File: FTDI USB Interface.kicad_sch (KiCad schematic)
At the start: 31 parts, among them U3 93LCxxA, U4 ASDMB-xxxMHz, U5 FT2232HQ

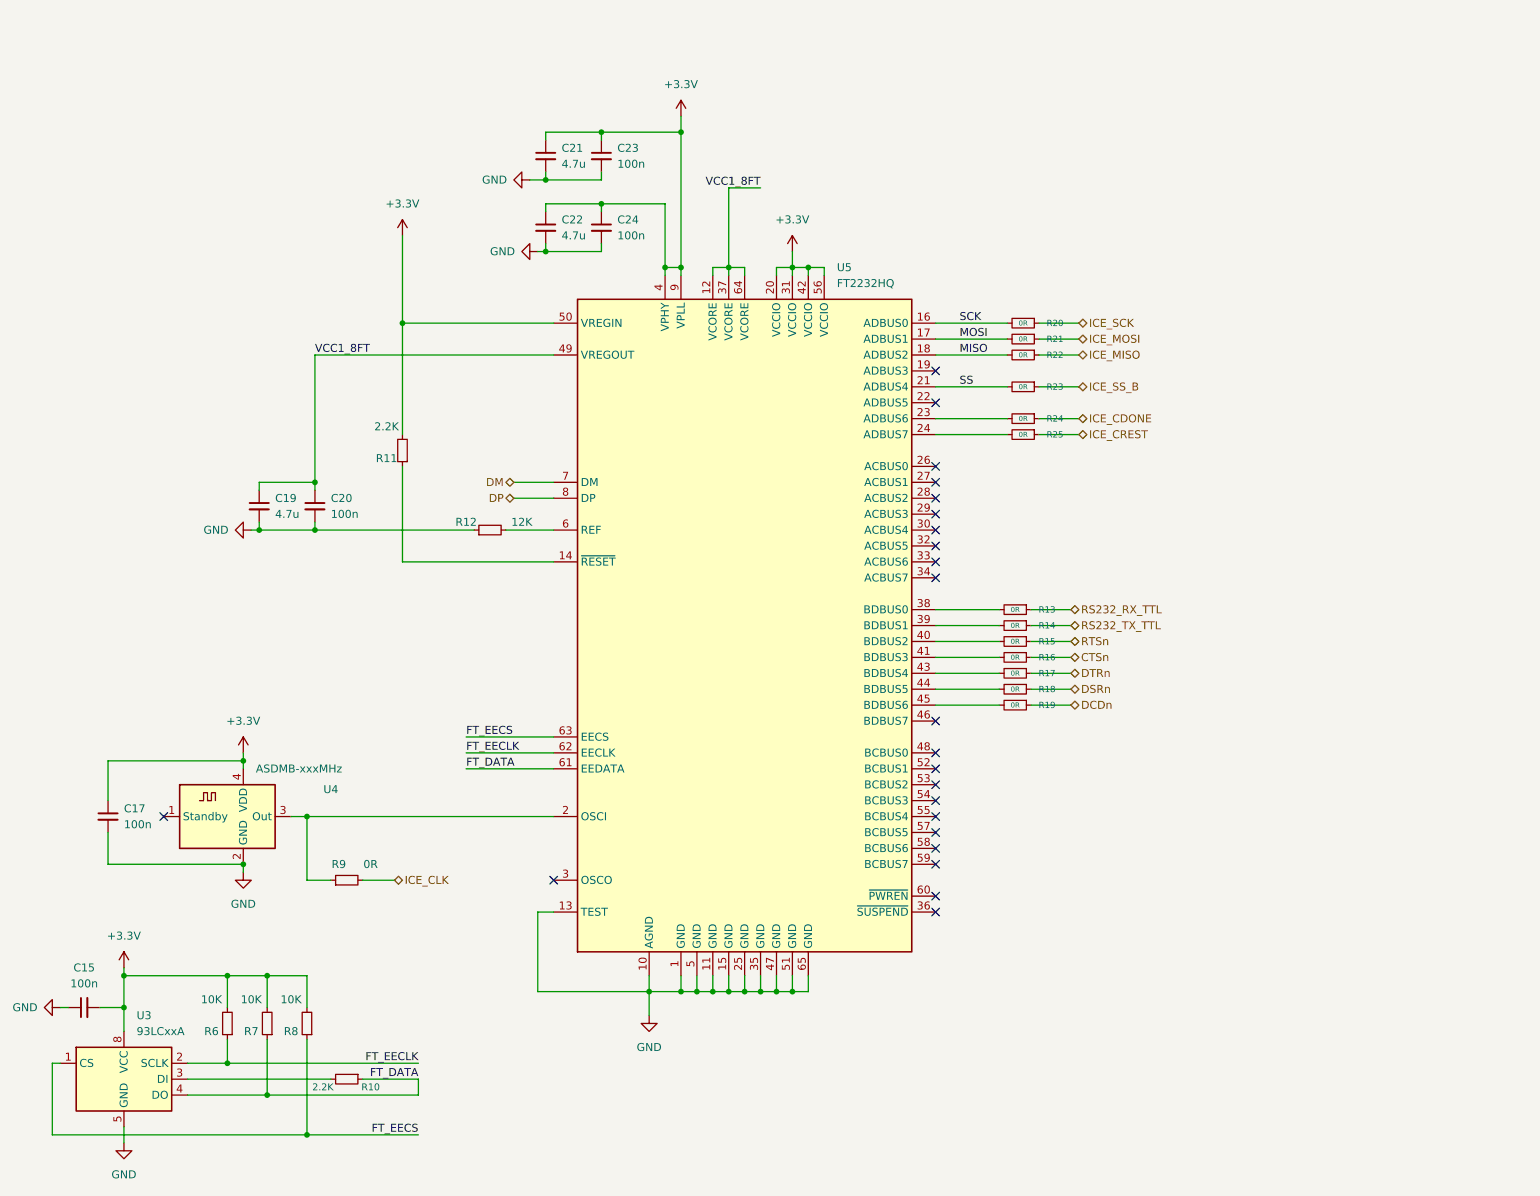
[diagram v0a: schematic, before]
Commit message: Update the description
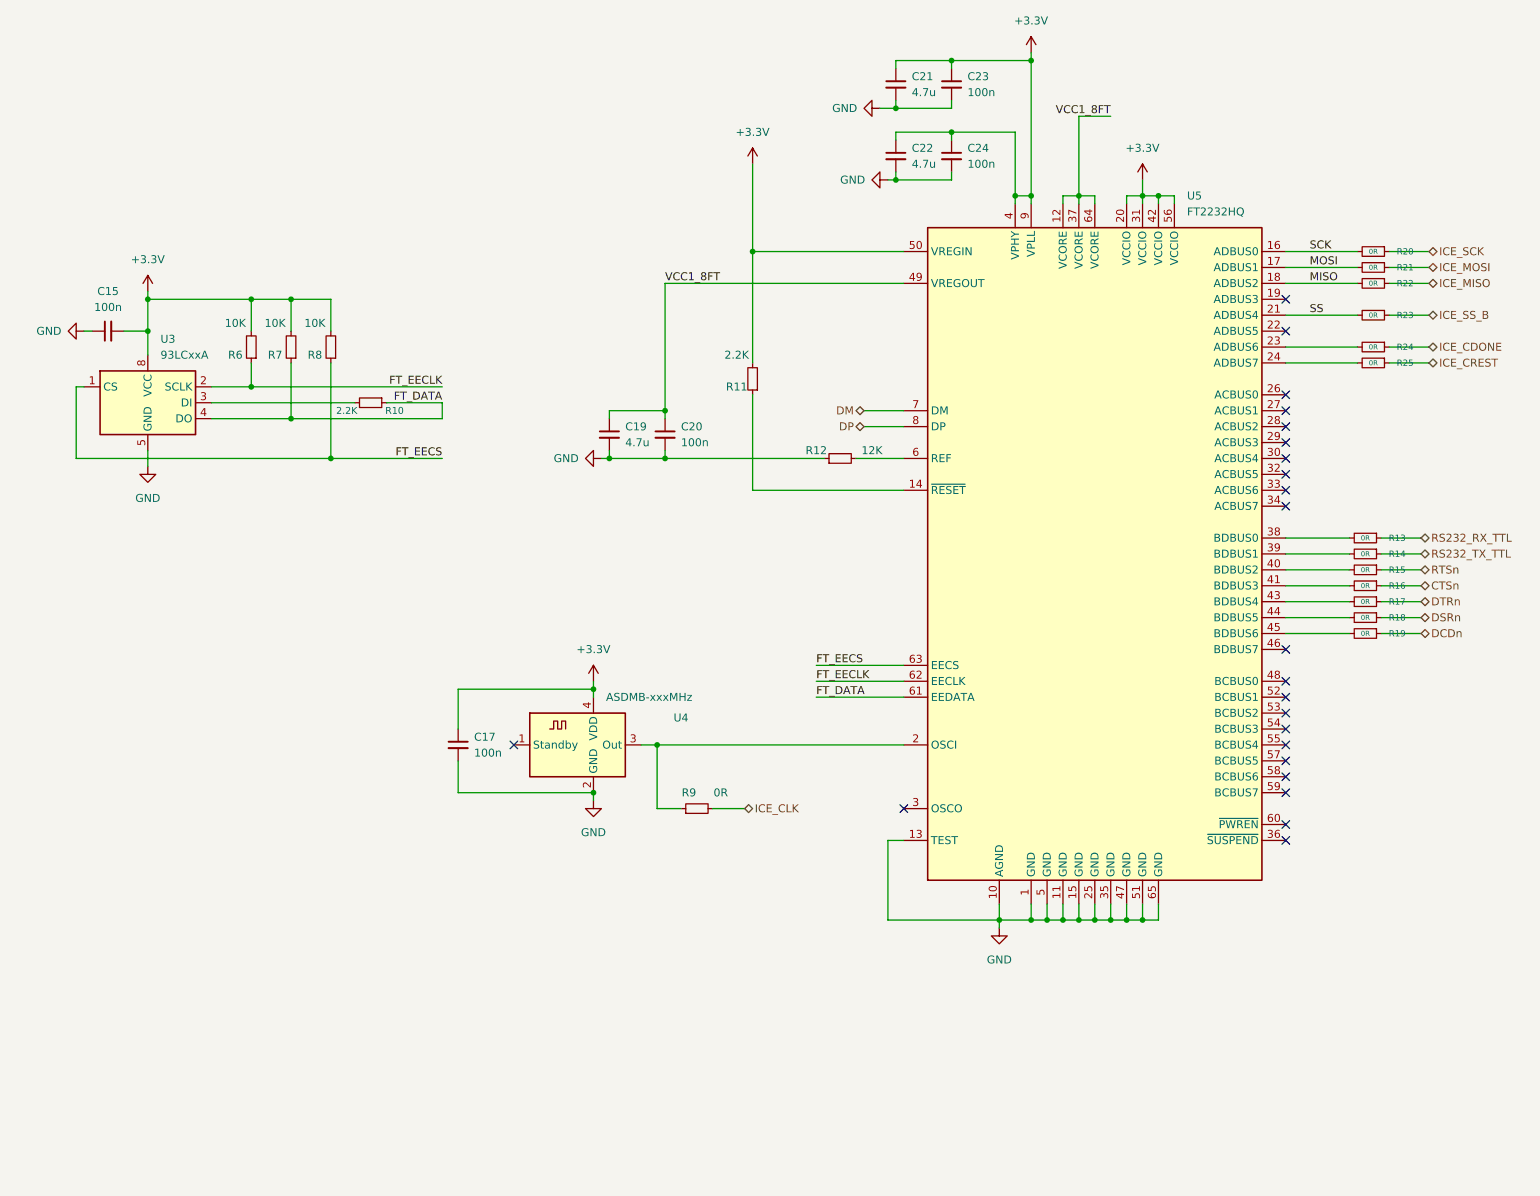
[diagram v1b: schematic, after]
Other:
- moved on the sheet: C15, C17, C19, C20, C21, C22, C23, C24, R10, R11, R12, R13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
